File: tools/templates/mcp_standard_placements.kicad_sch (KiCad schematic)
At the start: 150 parts, among them J1 ICSP, J3 PIR BOARD, J5 MOTOR, J6 DNP, Q1 FMOS3401A?, Q11 MMBTA55?, Q2 BC847B?, Q3 MMBTA55?, Q4 MMBTA55?, Q5 MMBTA55?, Q6 MMBTA55?, Q7 BC857C?, Q8 N/P pair? (372A), Q9 DNP, U1 S-1200B45? [pins], U106 U6A / DNP, U2 SN74LVC2G14DBV?, U3 SGM8542XS, U4 PIC16F18855, U5 MX512H, U6 S-812C33AMC? / 3.3V, U7 DNP, Y1 20 MHz

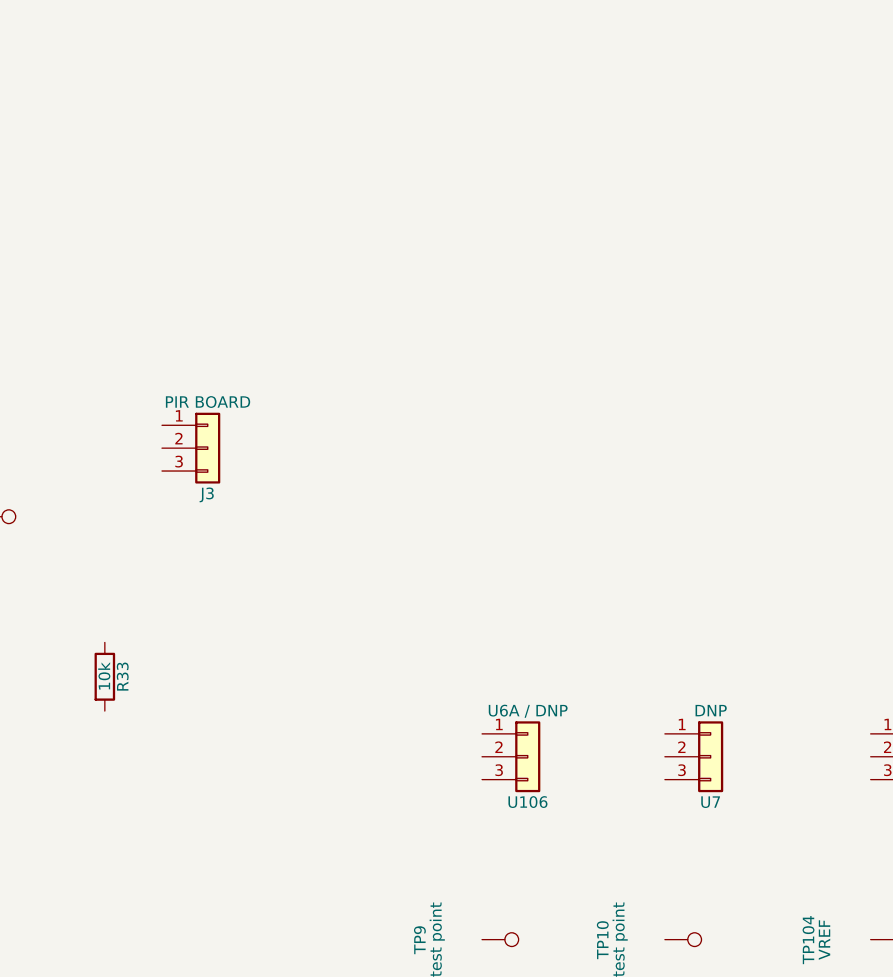
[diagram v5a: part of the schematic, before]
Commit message: Map U7 PIR connector and correct RB0 signal route
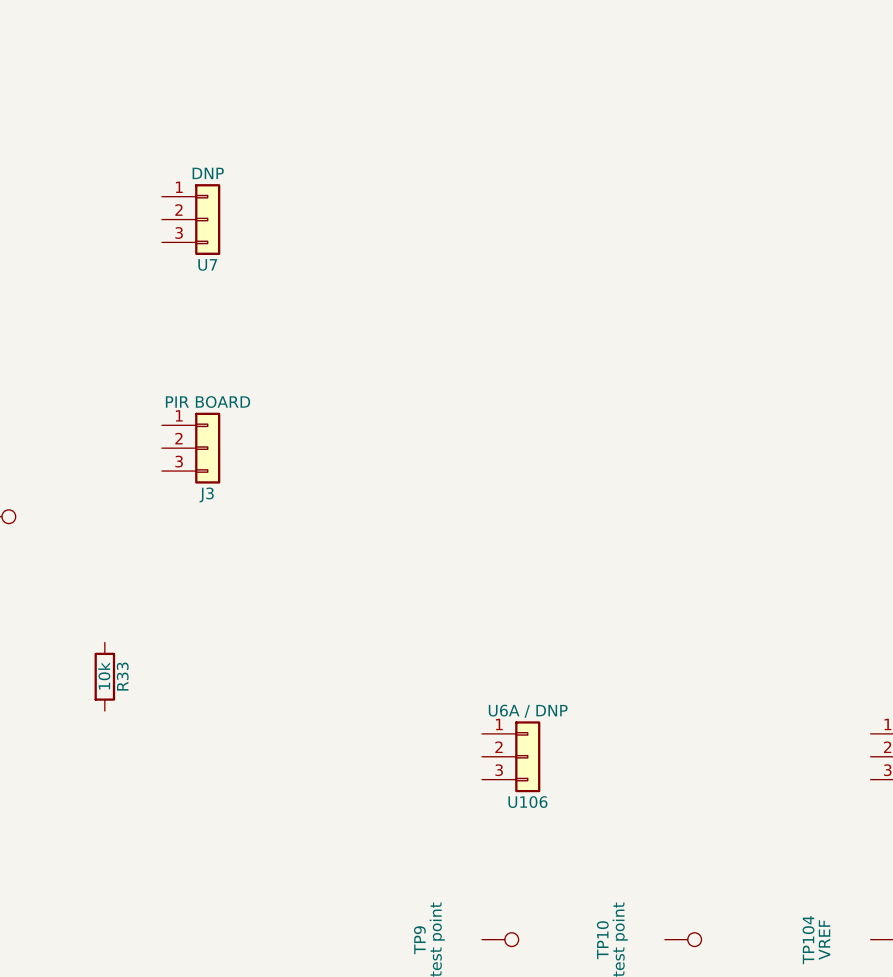
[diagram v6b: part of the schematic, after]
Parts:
- J3: MeasurementEvidence v0.9.14 user: pin1 PIR supply previously confirmed; pin2 H-R38 K/right/model1 1 ohm and H-R38 J/left/model2 10 kohm; pin3-GND 1 ohm. Pin2-GND remains 290 kohm (batch1), distinct from ground. Q2 onward/controller route remains unverified. -> v0.9.14 user: pin1 PIR supply previously confirmed; pin2 H-R38 K/right/model1 1 ohm and H-R38 J/left/model2 10 kohm; pin3-GND 1 ohm. Pin2-GND remains 290 kohm (batch1), distinct from ground. Q2 onward/controller route remains unverified. v0.9.16: matching physical columns reach U7; J3.1-U7.3 supply, J3.2-U7.2 signal, J3.3-U7.1 GND.; ViaEvidence v0.9.14 user: pin1 PIR supply previously confirmed; pin2 H-R38 K/right/model1 1 ohm and H-R38 J/left/model2 10 kohm; pin3-GND 1 ohm. Pin2-GND remains 290 kohm (batch1), distinct from ground. Q2 onward/controller route remains unverified. -> v0.9.14 user: pin1 PIR supply previously confirmed; pin2 H-R38 K/right/model1 1 ohm and H-R38 J/left/model2 10 kohm; pin3-GND 1 ohm. Pin2-GND remains 290 kohm (batch1), distinct from ground. Q2 onward/controller route remains unverified. v0.9.16: matching physical columns reach U7; J3.1-U7.3 supply, J3.2-U7.2 signal, J3.3-U7.1 GND.
- R21, R48: MeasurementEvidence (none) -> v0.9.16 CORRECTION: user confirms PIC21/RB0 -> TP16 -> Q2 s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; ViaEvidence v0.9.8: User confirms V071-VREF. Earlier V071-R21.2 and V02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 -> v0.9.16 CORRECTION: user confirms PIC21/RB0 -> TP16 -> Q2 s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
- R22: MeasurementEvidence v0.9.14 user: E/right/model1-GND 1 ohm; D/left/model2-VREF 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 -> v0.9.16 CORRECTION: user confirms PIC21/RB0 -> TP16 -> Q2 s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; ViaEvidence v0.9.14 user: E/right/model1-GND 1 ohm; D/left/model2-VREF 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 -> v0.9.16 CORRECTION: user confirms PIC21/RB0 -> TP16 -> Q2 s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
- TP104, U4: MeasurementEvidence (none) -> v0.9.16 CORRECTION: user confirms PIC21/RB0 -> TP16 -> Q2 s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; ViaEvidence v0.9.9: User checked V035-VREF TP. Prior photo association 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 -> v0.9.16 CORRECTION: user confirms PIC21/RB0 -> TP16 -> Q2 s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
- TP16: MeasurementEvidence (none) -> v0.9.16 CORRECTION: user confirms PIC21/RB0 -> TP16 -> Q2 s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; ViaEvidence (none) -> v0.9.16 CORRECTION: user confirms PIC21/RB0 -> TP16 -> Q2 s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
- U7: MeasurementEvidence (none) -> v0.9.16: user measured U7 square pad/model1 to J3.3/GND; mi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; ViaEvidence (none) -> v0.9.16: user measured U7 square pad/model1 to J3.3/GND; mi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
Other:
- moved on the sheet: U7
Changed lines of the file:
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@@
 			)
 		)
-		(property "ViaEvidence" "v0.9.9: User checked V035-VREF TP. Prior photo association V035-PIC4/RA2-C39.1 retained; joins the already confirmed RB0/V026/R21.2/V071 VREF node. No voltage or numerical resistance supplied. Other modeled bias branches retain earlier inferred status. V042-PIC20 supply now user-confirmed to board VDD/TP103, not motor VDD."
+		(property "ViaEvidence" "v0.9.16 CORRECTION: user confirms PIC21/RB0 -> TP16 -> Q2 single pad; TP16-VREF = 0.8 Mohm. User explicitly withdraws PIC21-VREF. PIC21/V026 belongs to H_PIR_SIG, separate from VREF. RA2/V035 and R21/V071 remain VREF. This supersedes every earlier RB0/V026-to-VREF statement."
 			(at 262.89 78.74 0)
 			(effects
 				(font
 					(size 1.27 1.27)
-				)
-				(hide yes)
-			)
+				) (hide yes))
 		)
+    (property "MeasurementEvidence" "v0.9.16 CORRECTION: user confirms PIC21/RB0 -> TP16 -> Q2 single pad; TP16-VREF = 0.8 Mohm. User explicitly withdraws PIC21-VREF. PIC21/V026 belongs to H_PIR_SIG, separate from VREF. RA2/V035 and R21/V071 remain VREF. This supersedes every earlier RB0/V026-to-VREF statement." (at 262.89 78.74 0)
+      (effects (font (size 1.27 1.27)) (hide yes))
+    )
 		(pin "1"
 		)
@@
 			)
 		)
-		(property "ViaEvidence" "v0.9.8: User confirms V071-VREF. Earlier V071-R21.2 and V026-VREF-PIC21/RB0 associations retained. R21.2 joins VREF. Existing R22.2/R23.2/R48.2 receiver-bias branches remain prior photo/circuit hypotheses, not new measured connections. VREF remains separate from VDD and RC1/V053. No voltage or numeric resistance supplied."
+		(property "ViaEvidence" "v0.9.16 CORRECTION: user confirms PIC21/RB0 -> TP16 -> Q2 single pad; TP16-VREF = 0.8 Mohm. User explicitly withdraws PIC21-VREF. PIC21/V026 belongs to H_PIR_SIG, separate from VREF. RA2/V035 and R21/V071 remain VREF. This supersedes every earlier RB0/V026-to-VREF statement."
 			(at 356.87 223.52 0)
 			(effects
 				(font
 					(size 1.27 1.27)
-				)
-				(hide yes)
-			)
+				) (hide yes))
 		)
+    (property "MeasurementEvidence" "v0.9.16 CORRECTION: user confirms PIC21/RB0 -> TP16 -> Q2 single pad; TP16-VREF = 0.8 Mohm. User explicitly withdraws PIC21-VREF. PIC21/V026 belongs to H_PIR_SIG, separate from VREF. RA2/V035 and R21/V071 remain VREF. This supersedes every earlier RB0/V026-to-VREF statement." (at 356.87 223.52 0)
+      (effects (font (size 1.27 1.27)) (hide yes))
+    )
 		(pin "1"
 		)
@@
 			)
 		)
-		(property "ViaEvidence" "v0.9.8: User confirms V071-VREF. Earlier V071-R21.2 and V026-VREF-PIC21/RB0 associations retained. R21.2 joins VREF. Existing R22.2/R23.2/R48.2 receiver-bias branches remain prior photo/circuit hypotheses, not new measured connections. VREF remains separate from VDD and RC1/V053. No voltage or numeric resistance supplied."
+		(property "ViaEvidence" "v0.9.16 CORRECTION: user confirms PIC21/RB0 -> TP16 -> Q2 single pad; TP16-VREF = 0.8 Mohm. User explicitly withdraws PIC21-VREF. PIC21/V026 belongs to H_PIR_SIG, separate from VREF. RA2/V035 and R21/V071 remain VREF. This supersedes every earlier RB0/V026-to-VREF statement."
 			(at 307.34 229.87 0)
 			(effects
 				(font
 					(size 1.27 1.27)
-				)
-				(hide yes)
-			)
+				) (hide yes))
 		)
+    (property "MeasurementEvidence" "v0.9.16 CORRECTION: user confirms PIC21/RB0 -> TP16 -> Q2 single pad; TP16-VREF = 0.8 Mohm. User explicitly withdraws PIC21-VREF. PIC21/V026 belongs to H_PIR_SIG, separate from VREF. RA2/V035 and R21/V071 remain VREF. This supersedes every earlier RB0/V026-to-VREF statement." (at 307.34 229.87 0)
+      (effects (font (size 1.27 1.27)) (hide yes))
+    )
 		(pin "1"
 		)
@@
 			)
 		)
-		(property "ViaEvidence" "v0.9.14 user: E/right/model1-GND 1 ohm; D/left/model2-VREF confirmed in batch1. R22 spans VREF to GND; 10 kohm agrees with 01C marking. U3 pin6 to E is 400 kohm and is not a wire."
+		(property "ViaEvidence" "v0.9.16 CORRECTION: user confirms PIC21/RB0 -> TP16 -> Q2 single pad; TP16-VREF = 0.8 Mohm. User explicitly withdraws PIC21-VREF. PIC21/V026 belongs to H_PIR_SIG, separate from VREF. RA2/V035 and R21/V071 remain VREF. This supersedes every earlier RB0/V026-to-VREF statement."
 			(at 326.39 229.87 0)
 			(effects
 				(font
 					(size 1.27 1.27)
-				)
-				(hide yes)
-			)
+				) (hide yes))
 		)
-		(property "MeasurementEvidence" "v0.9.14 user: E/right/model1-GND 1 ohm; D/left/model2-VREF confirmed in batch1. R22 spans VREF to GND; 10 kohm agrees with 01C marking. U3 pin6 to E is 400 kohm and is not a wire."
+		(property "MeasurementEvidence" "v0.9.16 CORRECTION: user confirms PIC21/RB0 -> TP16 -> Q2 single pad; TP16-VREF = 0.8 Mohm. User explicitly withdraws PIC21-VREF. PIC21/V026 belongs to H_PIR_SIG, separate from VREF. RA2/V035 and R21/V071 remain VREF. This supersedes every earlier RB0/V026-to-VREF statement."
 			(at 326.39 229.87 0)
 			(effects
 				(font
 					(size 1.27 1.27)
-				)
-				(hide yes)
-			)
+				) (hide yes))
 		)
 		(pin "1"
@@
 			)
 		)
-		(property "ViaEvidence" "v0.9.14 user: pin1 PIR supply previously confirmed; pin2 H-R38 K/right/model1 1 ohm and H-R38 J/left/model2 10 kohm; pin3-GND 1 ohm. Pin2-GND remains 290 kohm (batch1), distinct from ground. Q2 onward/controller route remains unverified."
+		(property "ViaEvidence" "v0.9.14 user: pin1 PIR supply previously confirmed; pin2 H-R38 K/right/model1 1 ohm and H-R38 J/left/model2 10 kohm; pin3-GND 1 ohm. Pin2-GND remains 290 kohm (batch1), distinct from ground. Q2 onward/controller route remains unverified. v0.9.16: matching physical columns reach U7; J3.1-U7.3 supply, J3.2-U7.2 signal, J3.3-U7.1 GND."
 			(at 405.13 327.66 0)
 			(effects
@@
 			)
 		)
-		(property "MeasurementEvidence" "v0.9.14 user: pin1 PIR supply previously confirmed; pin2 H-R38 K/right/model1 1 ohm and H-R38 J/left/model2 10 kohm; pin3-GND 1 ohm. Pin2-GND remains 290 kohm (batch1), distinct from ground. Q2 onward/controller route remains unverified."
+		(property "MeasurementEvidence" "v0.9.14 user: pin1 PIR supply previously confirmed; pin2 H-R38 K/right/model1 1 ohm and H-R38 J/left/model2 10 kohm; pin3-GND 1 ohm. Pin2-GND remains 290 kohm (batch1), distinct from ground. Q2 onward/controller route remains unverified. v0.9.16: matching physical columns reach U7; J3.1-U7.3 supply, J3.2-U7.2 signal, J3.3-U7.1 GND."
 			(at 405.13 327.66 0)
 			(effects
@@
 			)
 		)
+		(property "MeasurementEvidence" "v0.9.16 CORRECTION: user confirms PIC21/RB0 -> TP16 -> Q2 single pad; TP16-VREF = 0.8 Mohm. User explicitly withdraws PIC21-VREF. PIC21/V026 belongs to H_PIR_SIG, separate from VREF. RA2/V035 and R21/V071 remain VREF. This supersedes every earlier RB0/V026-to-VREF statement."
+			(at 379.73 335.28 0)
+			(effects
+				(font
+					(size 1.27 1.27)
+				) (hide yes))
+		)
+    (property "ViaEvidence" "v0.9.16 CORRECTION: user confirms PIC21/RB0 -> TP16 -> Q2 single pad; TP16-VREF = 0.8 Mohm. User explicitly withdraws PIC21-VREF. PIC21/V026 belongs to H_PIR_SIG, separate from VREF. RA2/V035 and R21/V071 remain VREF. This supersedes every earlier RB0/V026-to-VREF statement." (at 379.73 335.28 0)
+      (effects (font (size 1.27 1.27)) (hide yes))
+    )
 		(pin "1"
 		)
@@
 	(symbol
 		(lib_id "Connector_Generic:Conn_01x03")
-		(at 461.01 361.95 0)
+		(at 405.13 302.26 0)
 		(unit 1)
 		(body_style 1)
@@
 		(dnp no)
 		(property "Reference" "U7"
-			(at 461.01 367.03 0)
+			(at 405.13 307.34 0)
 			(show_name no)
 			(do_not_autoplace no)
@@
 		)
 		(property "Value" "DNP"
-			(at 461.01 356.87 0)
+			(at 405.13 297.18 0)
 			(show_name no)
 			(do_not_autoplace no)
@@
 		)
 		(property "Footprint" "Connector_PinHeader_2.54mm:PinHeader_1x03_P2.54mm_Vertical"
-			(at 461.01 361.95 0)
+			(at 405.13 302.26 0)
 			(hide yes)
 			(show_name no)
@@
 		)
 		(property "Datasheet" ""
-			(at 461.01 361.95 0)
+			(at 405.13 302.26 0)
 			(hide yes)
 			(show_name no)
@@
 		)
 		(property "Description" "Generic connector, single row, 01x03, script generated (kicad-library-utils/schlib/autogen/connector/)"
-			(at 461.01 361.95 0)
+			(at 405.13 302.26 0)
 			(hide yes)
 			(show_name no)
@@
 			)
 		)
+		(property "MeasurementEvidence" "v0.9.16: user measured U7 square pad/model1 to J3.3/GND; middle/model2 to J3.2/H_PIR_RAW; outer round/model3 to J3.1/H_PIR_VDD. IMG_2441 confirms square-pad numbering. No numerical continuity values supplied. Empty option remains DNP."
+			(at 405.13 302.26 0)
+			(effects
+				(font
+					(size 1.27 1.27)
+				)
+				(hide yes)
+			)
+		)
+		(property "ViaEvidence" "v0.9.16: user measured U7 square pad/model1 to J3.3/GND; middle/model2 to J3.2/H_PIR_RAW; outer round/model3 to J3.1/H_PIR_VDD. IMG_2441 confirms square-pad numbering. No numerical continuity values supplied. Empty option remains DNP."
+			(at 405.13 302.26 0)
+			(effects
+				(font
+					(size 1.27 1.27)
+				)
+				(hide yes)
+			)
+		)
 		(pin "1"
 		)
@@
 			)
 		)
-		(property "ViaEvidence" "v0.9.9: User checked V035-VREF TP. Prior photo association V035-PIC4/RA2-C39.1 retained; joins the already confirmed RB0/V026/R21.2/V071 VREF node. No voltage or numerical resistance supplied. Other modeled bias branches retain earlier inferred status."
+		(property "ViaEvidence" "v0.9.16 CORRECTION: user confirms PIC21/RB0 -> TP16 -> Q2 single pad; TP16-VREF = 0.8 Mohm. User explicitly withdraws PIC21-VREF. PIC21/V026 belongs to H_PIR_SIG, separate from VREF. RA2/V035 and R21/V071 remain VREF. This supersedes every earlier RB0/V026-to-VREF statement."
 			(at 478.79 382.27 0)
 			(effects
 				(font
 					(size 1.27 1.27)
-				)
-				(hide yes)
-			)
+				) (hide yes))
 		)
+    (property "MeasurementEvidence" "v0.9.16 CORRECTION: user confirms PIC21/RB0 -> TP16 -> Q2 single pad; TP16-VREF = 0.8 Mohm. User explicitly withdraws PIC21-VREF. PIC21/V026 belongs to H_PIR_SIG, separate from VREF. RA2/V035 and R21/V071 remain VREF. This supersedes every earlier RB0/V026-to-VREF statement." (at 478.79 382.27 0)
+      (effects (font (size 1.27 1.27)) (hide yes))
+    )
 		(pin "1"
 		)
